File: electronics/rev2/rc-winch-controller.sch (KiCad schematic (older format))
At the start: 14 parts, among them J1 Conn_01x06, J2 Conn_01x06, SW1 SETUP, U1 MCP1703A-3302_SOT23, U2 LPC812M001JDH16, U3 RZ7889

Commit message: Update PCB
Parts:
- removed C4: CP, Capacitor_THT:CP_Axial_L11.0mm_D6.0mm_P18.00mm_Horizontal, symbol Device:CP
- C1, C2: footprint Capacitor_SMD:C_0805_2012Metric_Pad1.18x1.45mm_HandSolder -> Capacitor_SMD:C_0805_2012Metric
- C3: footprint Capacitor_SMD:C_0603_1608Metric_Pad1.08x0.95mm_HandSolder -> Capacitor_SMD:C_0603_1608Metric
- D1: footprint Package_TO_SOT_SMD:SOT-523 -> Package_TO_SOT_SMD:SOT-23
- U1: footprint Package_TO_SOT_SMD:SOT-23_Handsoldering -> Package_TO_SOT_SMD:SOT-23W
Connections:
- net GND: now also J1.5 (Pin_5)
- net LED-A: now also RN1.1 (R1.1); no longer RN1.3 (R3.1)
- net LED-B: now also U2.6 (PIO0_2); no longer U2.9 (PIO0_1)
- net LED-G: now also U2.5 (PIO0_3); no longer U2.6 (PIO0_2)
- net LED-R: now also U2.1 (PIO0_13); no longer U2.5 (PIO0_3)
- net MOT1: now also J2.2 (Pin_2); no longer J2.1 (Pin_1)
- net MOT2: now also J2.1 (Pin_1); no longer J2.2 (Pin_2)
- net Tx: now also RN1.5 (R4.2); no longer RN1.8 (R1.2)
- net Tx-in: now also RN1.4 (R4.1); no longer RN1.1 (R1.1)
- net VDD: now also RN1.8 (R1.2); no longer RN1.6 (R3.2)
- net VMOT: now also J1.6 (Pin_6)
- net ST-Rx renamed AUX-Rx
- net AUX-Rx: now also RN1.6 (R3.2); no longer RN1.5 (R4.2)
- net ST-Rx-in renamed AUX-Rx-in
- net AUX-Rx-in: now also RN1.3 (R3.1); no longer RN1.4 (R4.1)
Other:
- note added: "Pin 5+6 to connect 100uF/16V polymer"
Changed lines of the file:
@@
 F 0 "U1" H 2400 1742 50  0000 C CNN
 F 1 "MCP1703A-3302_SOT23" H 2400 1651 50  0000 C CNN
-F 2 "Package_TO_SOT_SMD:SOT-23_Handsoldering" H 2400 1700 50  0001 C CNN
+F 2 "Package_TO_SOT_SMD:SOT-23W" H 2400 1700 50  0001 C CNN
 F 3 "http://ww1.microchip.com/downloads/en/DeviceDoc/20005122B.pdf" H 2400 1450 50  0001 C CNN
 	1    2400 1500
 	1    0    0    -1
-$EndComp
-$Comp
-L Device:CP C4
-U 1 1 600D9E9B
-P 8000 2800
-F 0 "C4" H 7882 2754 50  0000 R CNN
-F 1 "CP" H 7882 2845 50  0000 R CNN
-F 2 "Capacitor_THT:CP_Axial_L11.0mm_D6.0mm_P18.00mm_Horizontal" H 8038 2650 50  0001 C CNN
-F 3 "~" H 8000 2800 50  0001 C CNN
-	1    8000 2800
-	-1   0    0    1
 $EndComp
 $Comp
@@
 F 0 "C1" H 1865 1696 50  0000 L CNN
 F 1 "1u" H 1865 1605 50  0000 L CNN
-F 2 "Capacitor_SMD:C_0805_2012Metric_Pad1.18x1.45mm_HandSolder" H 1788 1500 50  0001 C CNN
+F 2 "Capacitor_SMD:C_0805_2012Metric" H 1788 1500 50  0001 C CNN
 F 3 "~" H 1750 1650 50  0001 C CNN
 	1    1750 1650
@@
 F 0 "C2" H 3165 1696 50  0000 L CNN
 F 1 "10u" H 3165 1605 50  0000 L CNN
-F 2 "Capacitor_SMD:C_0805_2012Metric_Pad1.18x1.45mm_HandSolder" H 3088 1500 50  0001 C CNN
+F 2 "Capacitor_SMD:C_0805_2012Metric" H 3088 1500 50  0001 C CNN
 F 3 "~" H 3050 1650 50  0001 C CNN
 	1    3050 1650
@@
 F 0 "C3" H 3565 1696 50  0000 L CNN
 F 1 "100n" H 3565 1605 50  0000 L CNN
-F 2 "Capacitor_SMD:C_0603_1608Metric_Pad1.08x0.95mm_HandSolder" H 3488 1500 50  0001 C CNN
+F 2 "Capacitor_SMD:C_0603_1608Metric" H 3488 1500 50  0001 C CNN
 F 3 "~" H 3450 1650 50  0001 C CNN
 	1    3450 1650
@@
 $EndComp
 Wire Wire Line
-	6500 5200 6050 5200
-Wire Wire Line
-	6050 5300 6350 5300
-Wire Wire Line
-	6900 5200 7450 5200
-Wire Wire Line
-	7450 5300 7000 5300
+	6500 5200 6350 5200
+Wire Wire Line
+	6900 5200 7000 5200
 Wire Wire Line
 	4150 3250 3600 3250
 Text Label 3600 3250 0    50   ~ 0
-ST-Rx
+AUX-Rx
 Wire Wire Line
 	4150 3650 3600 3650
@@
 Wire Wire Line
 	7400 2950 7400 3050
-Connection ~ 8000 2950
-Wire Wire Line
-	8000 2950 7400 2950
-$Comp
-L power:GND #PWR09
-U 1 1 600FB047
-P 8000 2550
-F 0 "#PWR09" H 8000 2300 50  0001 C CNN
-F 1 "GND" H 8005 2377 50  0000 C CNN
-F 2 "" H 8000 2550 50  0001 C CNN
-F 3 "" H 8000 2550 50  0001 C CNN
-	1    8000 2550
-	-1   0    0    1
-$EndComp
-Wire Wire Line
-	8000 2550 8000 2650
 $Comp
 L Device:D_Schottky_x2_KCom_AAK D1
@@
 F 0 "D1" H 1750 1167 50  0000 C CNN
 F 1 "D_Schottky_x2_KCom_AAK" H 1750 1076 50  0000 C CNN
-F 2 "Package_TO_SOT_SMD:SOT-523" H 1750 950 50  0001 C CNN
+F 2 "Package_TO_SOT_SMD:SOT-23" H 1750 950 50  0001 C CNN
 F 3 "~" H 1750 950 50  0001 C CNN
 	1    1750 950
@@
 Text Label 1100 950  0    50   ~ 0
 VMOT
-Text Label 7500 2950 0    50   ~ 0
+Text Label 7950 2950 0    50   ~ 0
 VMOT
 Wire Wire Line
@@
 Wire Wire Line
 	7400 3950 7400 4050
-Wire Wire Line
-	6900 5400 7000 5400
-Wire Wire Line
-	6500 5400 6350 5400
-Text Label 6050 5300 0    50   ~ 0
+Text Label 6050 5200 0    50   ~ 0
 LED-A
 Wire Wire Line
@@
 Wire Wire Line
 	3600 3450 4150 3450
+Text Label 3600 3550 0    50   ~ 0
+LED-G
+Text Label 6150 3850 2    50   ~ 0
+LED-R
 Text Label 3600 3450 0    50   ~ 0
-LED-G
-Text Label 3600 3550 0    50   ~ 0
-LED-R
-Wire Wire Line
-	3600 3350 4150 3350
-Text Label 3600 3350 0    50   ~ 0
 LED-B
 Text Label 4200 1500 0    50   ~ 0
 VDD
-Text Label 7450 5300 2    50   ~ 0
+Text Label 7450 5200 2    50   ~ 0
 VDD
+Text Label 6050 5400 0    50   ~ 0
+AUX-Rx-in
 Text Label 6050 5500 0    50   ~ 0
-ST-Rx-in
-Text Label 6050 5200 0    50   ~ 0
 Tx-in
+Text Label 7450 5400 2    50   ~ 0
+AUX-Rx
 Text Label 7450 5500 2    50   ~ 0
-ST-Rx
-Text Label 7450 5200 2    50   ~ 0
 Tx
 Wire Wire Line
@@
 	1950 3150 1350 3150
 Text Label 1950 3250 2    50   ~ 0
-ST-Rx-in
+AUX-Rx-in
 Text Label 1950 3150 2    50   ~ 0
 Tx-in
@@
 	0    1    1    0
 $EndComp
-Wire Wire Line
-	8500 2950 8000 2950
-NoConn ~ 1350 3050
 Text Label 9150 2950 0    50   ~ 0
 VMOT-in
 Text Notes 5800 5750 0    50   ~ 0
 2x 1k in parallel to get detect LED current
-NoConn ~ 1350 2950
 Wire Wire Line
 	7800 3350 7900 3350
@@
 U 1 1 6019C61D
 P 7400 3450
-F 0 "U3" H 7400 4031 50  0000 C CNN
-F 1 "RZ7889" H 7400 3940 50  0000 C CNN
+F 0 "U3" H 7650 3800 50  0000 C CNN
+F 1 "RZ7889" H 7150 3800 50  0000 C CNN
 F 2 "Package_SO:SOIC-8-1EP_3.9x4.9mm_P1.27mm_EP2.29x3mm_ThermalVias" H 7400 2900 50  0001 C CNN
 F 3 "" H 7100 3800 50  0001 C CNN
@@
 Text Label 6450 3250 0    50   ~ 0
 FWD
-Wire Wire Line
-	8650 3250 8650 3350
-Wire Wire Line
-	8650 3350 9550 3350
-Wire Wire Line
-	7900 3250 8650 3250
 Connection ~ 7900 3250
-Wire Wire Line
-	9550 3250 8850 3250
-Wire Wire Line
-	8850 3250 8850 3450
 Wire Wire Line
 	8850 3450 8100 3450
@@
 LED-A
 Wire Wire Line
-	6350 5400 6350 5300
-Connection ~ 6350 5300
-Wire Wire Line
 	6350 5300 6500 5300
 Wire Wire Line
 	6050 5500 6500 5500
 Wire Wire Line
-	7000 5400 7000 5300
-Connection ~ 7000 5300
-Wire Wire Line
 	7000 5300 6900 5300
 Wire Wire Line
 	6900 5500 7450 5500
+Wire Wire Line
+	1350 3050 1500 3050
+Wire Wire Line
+	1500 3050 1500 3450
+Connection ~ 1500 3450
+Wire Wire Line
+	1350 2950 1950 2950
+Text Label 1950 2950 2    50   ~ 0
+VMOT
+Wire Wire Line
+	7400 2950 8500 2950
+Text Notes 850  4050 0    50   ~ 0
+Pin 5+6 to connect 100uF/16V polymer
+Wire Wire Line
+	6350 5200 6350 5300
+Connection ~ 6350 5200
+Wire Wire Line
+	6350 5200 6050 5200
+Wire Wire Line
+	6050 5400 6500 5400
+Wire Wire Line
+	7000 5300 7000 5200
+Connection ~ 7000 5200
+Wire Wire Line
+	7000 5200 7450 5200
+Wire Wire Line
+	6900 5400 7450 5400
+Wire Wire Line
+	7900 3250 9550 3250
+Wire Wire Line
+	8850 3450 8850 3350
+Wire Wire Line
+	8850 3350 9550 3350
+Wire Wire Line
+	6150 3850 5550 3850
+NoConn ~ 4150 3350
+NoConn ~ 4150 3750
 $EndSCHEMATC

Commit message: Update layout and silkscreen
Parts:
- F1: value 3A 16V 1812 -> 4A 16V 1812
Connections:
- net AUX-Rx: now also RN1.5 (R4.2); no longer RN1.6 (R3.2)
- net AUX-Rx-in: now also RN1.4 (R4.1); no longer RN1.3 (R3.1)
- net Tx: now also RN1.6 (R3.2); no longer RN1.5 (R4.2)
- net Tx-in: now also RN1.3 (R3.1); no longer RN1.4 (R4.1)
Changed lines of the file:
@@
 Text Label 7450 5200 2    50   ~ 0
 VDD
+Text Label 6050 5500 0    50   ~ 0
+AUX-Rx-in
 Text Label 6050 5400 0    50   ~ 0
-AUX-Rx-in
-Text Label 6050 5500 0    50   ~ 0
 Tx-in
+Text Label 7450 5500 2    50   ~ 0
+AUX-Rx
 Text Label 7450 5400 2    50   ~ 0
-AUX-Rx
-Text Label 7450 5500 2    50   ~ 0
 Tx
 Wire Wire Line
@@
 P 8650 2950
 F 0 "F1" V 8425 2950 50  0000 C CNN
-F 1 "3A 16V 1812" V 8516 2950 50  0000 C CNN
+F 1 "4A 16V 1812" V 8516 2950 50  0000 C CNN
 F 2 "Fuse:Fuse_1812_4532Metric_Pad1.30x3.40mm_HandSolder" H 8700 2750 50  0001 L CNN
 F 3 "~" H 8650 2950 50  0001 C CNN

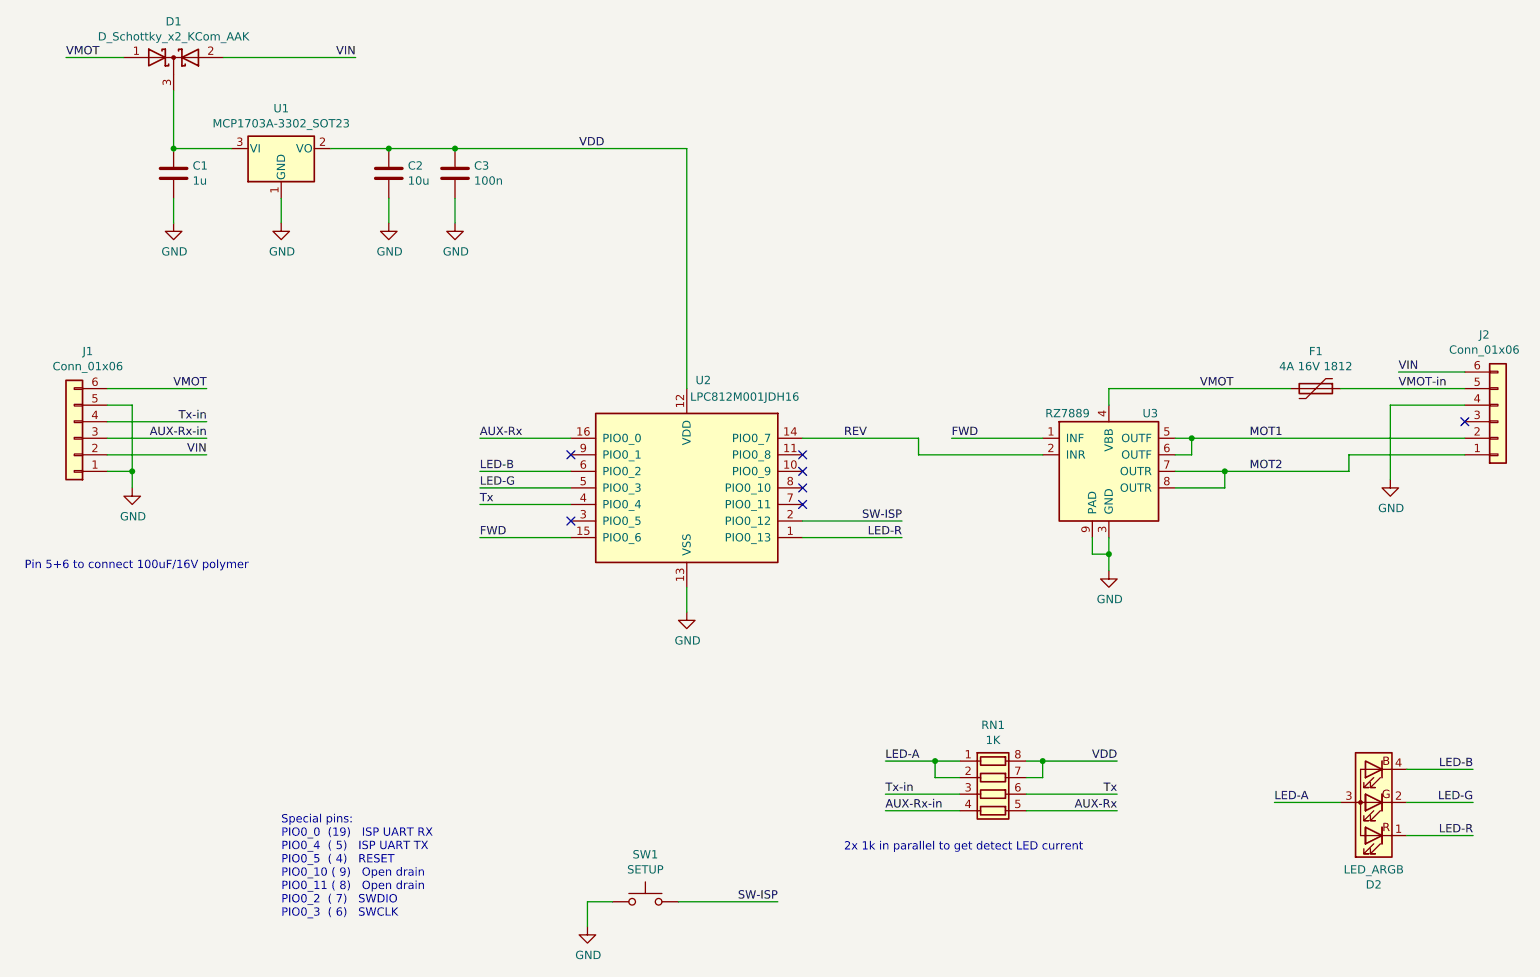
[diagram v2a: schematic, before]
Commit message: Change MCU to TSSOP 20 version
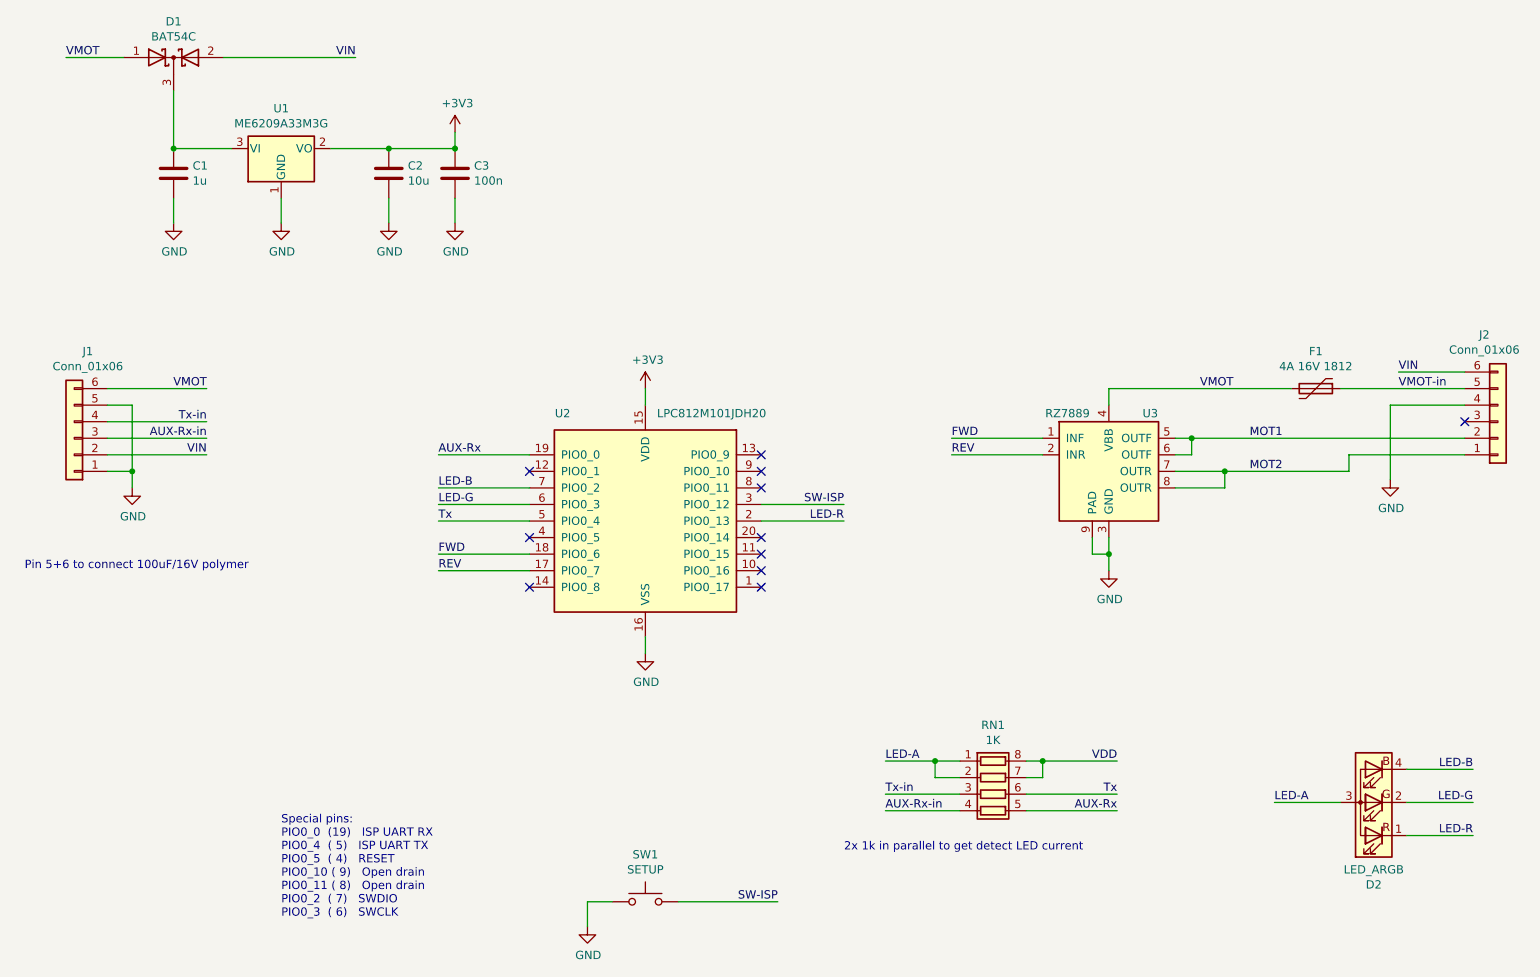
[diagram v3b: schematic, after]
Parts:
- removed U2: LPC812M001JDH16, Package_SO:TSSOP-16_4.4x5mm_P0.65mm, symbol MCU_NXP_LPC:LPC812M001JDH16
- added U2: LPC812M101JDH20, Package_SO:TSSOP-20_4.4x6.5mm_P0.65mm, symbol MCU_NXP_LPC:LPC812M101JDH20
- D1: value D_Schottky_x2_KCom_AAK -> BAT54C
- U1: value MCP1703A-3302_SOT23 -> ME6209A33M3G
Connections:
- net AUX-Rx: now also U2.19 (PIO0_0)
- net FWD: now also U2.18 (PIO0_6)
- net GND: now also U2.16 (VSS)
- net LED-B: now also U2.7 (PIO0_2)
- net LED-G: now also U2.6 (PIO0_3)
- net LED-R: now also U2.2 (PIO0_13)
- net REV: now also U2.17 (PIO0_7)
- net SW-ISP: now also U2.3 (PIO0_12)
- net Tx: now also U2.5 (PIO0_4)
- net VDD: no longer C2.1, C3.1, U1.2 (VO)
- new net +3V3: C2.1, C3.1, U1.2 (VO), U2.15 (VDD)
- no-connect marks 7 -> 11
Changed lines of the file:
@@
 Sheet 1 1
 Title "RC Winch Controller"
-Date "2021-01-24"
+Date "2021-02-11"
 Rev "Rev2"
 Comp "LANE Boys RC"
@@
 Comment4 ""
 $EndDescr
-$Comp
-L MCU_NXP_LPC:LPC812M001JDH16 U2
-U 1 1 600D3394
-P 4850 3550
-F 0 "U2" H 4950 4200 50  0000 C CNN
-F 1 "LPC812M001JDH16" H 5200 4100 50  0000 C CNN
-F 2 "Package_SO:TSSOP-16_4.4x5mm_P0.65mm" H 5800 4150 50  0001 C CNN
-F 3 "http://www.nxp.com/documents/data_sheet/LPC81XM.pdf" H 4850 3050 50  0001 C CNN
-	1    4850 3550
-	1    0    0    -1
-$EndComp
 $Comp
 L rc-winch-controller-parts:XINLIGHT_XL-2012RGBC D2
@@
 P 2400 1500
 F 0 "U1" H 2400 1742 50  0000 C CNN
-F 1 "MCP1703A-3302_SOT23" H 2400 1651 50  0000 C CNN
+F 1 "ME6209A33M3G" H 2400 1651 50  0000 C CNN
 F 2 "Package_TO_SOT_SMD:SOT-23W" H 2400 1700 50  0001 C CNN
 F 3 "http://ww1.microchip.com/downloads/en/DeviceDoc/20005122B.pdf" H 2400 1450 50  0001 C CNN
@@
 Wire Wire Line
 	6900 5200 7000 5200
-Wire Wire Line
-	4150 3250 3600 3250
-Text Label 3600 3250 0    50   ~ 0
-AUX-Rx
-Wire Wire Line
-	4150 3650 3600 3650
-Text Label 3600 3650 0    50   ~ 0
-Tx
-Wire Wire Line
-	5550 3750 6150 3750
-Text Label 6150 3750 2    50   ~ 0
-SW-ISP
-$Comp
-L power:GND #PWR07
-U 1 1 600ED009
-P 4850 4300
-F 0 "#PWR07" H 4850 4050 50  0001 C CNN
-F 1 "GND" H 4855 4127 50  0000 C CNN
-F 2 "" H 4850 4300 50  0001 C CNN
-F 3 "" H 4850 4300 50  0001 C CNN
-	1    4850 4300
-	1    0    0    -1
-$EndComp
-Wire Wire Line
-	4850 4150 4850 4300
 $Comp
 L power:GND #PWR06
@@
 Text Notes 2400 6150 0    50   ~ 0
 Special pins:\nPIO0_0  (19)   ISP UART RX\nPIO0_4  ( 5)   ISP UART TX\nPIO0_5  ( 4)   RESET\nPIO0_10 ( 9)   Open drain\nPIO0_11 ( 8)   Open drain\nPIO0_2  ( 7)   SWDIO\nPIO0_3  ( 6)   SWCLK
-Text Label 3600 3850 0    50   ~ 0
-FWD
-Text Label 5800 3250 0    50   ~ 0
-REV
 Wire Wire Line
 	7800 3250 7900 3250
@@
 P 1750 950
 F 0 "D1" H 1750 1167 50  0000 C CNN
-F 1 "D_Schottky_x2_KCom_AAK" H 1750 1076 50  0000 C CNN
+F 1 "BAT54C" H 1750 1076 50  0000 C CNN
 F 2 "Package_TO_SOT_SMD:SOT-23" H 1750 950 50  0001 C CNN
 F 3 "~" H 1750 950 50  0001 C CNN
@@
 Wire Wire Line
 	2700 1500 3050 1500
-Wire Wire Line
-	4850 1500 4850 2950
 Connection ~ 3050 1500
 Wire Wire Line
 	3050 1500 3450 1500
 Connection ~ 3450 1500
-Wire Wire Line
-	3450 1500 4850 1500
 Connection ~ 1750 1500
 $Comp
@@
 Text Label 9600 5250 2    50   ~ 0
 LED-B
-NoConn ~ 5550 3550
-NoConn ~ 5550 3650
-Wire Wire Line
-	4150 3550 3600 3550
-Wire Wire Line
-	3600 3450 4150 3450
-Text Label 3600 3550 0    50   ~ 0
-LED-G
-Text Label 6150 3850 2    50   ~ 0
-LED-R
-Text Label 3600 3450 0    50   ~ 0
-LED-B
-Text Label 4200 1500 0    50   ~ 0
-VDD
 Text Label 7450 5200 2    50   ~ 0
 VDD
@@
 $EndComp
 Wire Wire Line
-	3600 3850 4150 3850
-NoConn ~ 5550 3350
-NoConn ~ 5550 3450
-Wire Wire Line
-	5550 3250 6250 3250
-Wire Wire Line
-	6250 3250 6250 3350
-Wire Wire Line
-	6250 3350 7000 3350
+	6450 3350 7000 3350
 Wire Wire Line
 	6450 3250 7000 3250
@@
 Wire Wire Line
 	8850 3350 9550 3350
-Wire Wire Line
-	6150 3850 5550 3850
-NoConn ~ 4150 3350
-NoConn ~ 4150 3750
+$Comp
+L power:+3V3 #PWR?
+U 1 1 60252048
+P 3450 1400
+F 0 "#PWR?" H 3450 1250 50  0001 C CNN
+F 1 "+3V3" H 3465 1573 50  0000 C CNN
+F 2 "" H 3450 1400 50  0001 C CNN
+F 3 "" H 3450 1400 50  0001 C CNN
+	1    3450 1400
+	1    0    0    -1
+$EndComp
+Wire Wire Line
+	3450 1400 3450 1500
+Text Label 6450 3350 0    50   ~ 0
+REV
+$Comp
+L MCU_NXP_LPC:LPC812M101JDH20 U2
+U 1 1 60268FFA
+P 4600 3750
+F 0 "U2" H 4100 4400 50  0000 C CNN
+F 1 "LPC812M101JDH20" H 5000 4400 50  0000 C CNN
+F 2 "Package_SO:TSSOP-20_4.4x6.5mm_P0.65mm" H 5600 4450 50  0001 C CNN
+F 3 "http://www.nxp.com/documents/data_sheet/LPC81XM.pdf" H 4600 3250 50  0001 C CNN
+	1    4600 3750
+	1    0    0    -1
+$EndComp
+$Comp
+L power:+3V3 #PWR?
+U 1 1 6026DDF4
+P 4600 2950
+F 0 "#PWR?" H 4600 2800 50  0001 C CNN
+F 1 "+3V3" H 4615 3123 50  0000 C CNN
+F 2 "" H 4600 2950 50  0001 C CNN
+F 3 "" H 4600 2950 50  0001 C CNN
+	1    4600 2950
+	1    0    0    -1
+$EndComp
+Wire Wire Line
+	4600 2950 4600 3050
+$Comp
+L power:GND #PWR?
+U 1 1 6026FF95
+P 4600 4550
+F 0 "#PWR?" H 4600 4300 50  0001 C CNN
+F 1 "GND" H 4605 4377 50  0000 C CNN
+F 2 "" H 4600 4550 50  0001 C CNN
+F 3 "" H 4600 4550 50  0001 C CNN
+	1    4600 4550
+	1    0    0    -1
+$EndComp
+Wire Wire Line
+	4600 4450 4600 4550
+Wire Wire Line
+	3900 3350 3350 3350
+Text Label 3350 3350 0    50   ~ 0
+AUX-Rx
+Wire Wire Line
+	3900 3750 3350 3750
+Text Label 3350 3750 0    50   ~ 0
+Tx
+Text Label 3350 3950 0    50   ~ 0
+FWD
+Wire Wire Line
+	3900 3650 3350 3650
+Wire Wire Line
+	3350 3550 3900 3550
+Text Label 3350 3650 0    50   ~ 0
+LED-G
+Text Label 3350 3550 0    50   ~ 0
+LED-B
+Wire Wire Line
+	3350 3950 3900 3950
+Text Label 3350 4050 0    50   ~ 0
+REV
+Wire Wire Line
+	3900 4050 3350 4050
+NoConn ~ 3900 3450
+NoConn ~ 3900 3850
+NoConn ~ 3900 4150
+Wire Wire Line
+	5300 3650 5800 3650
+Text Label 5800 3650 2    50   ~ 0
+SW-ISP
+Text Label 5800 3750 2    50   ~ 0
+LED-R
+Wire Wire Line
+	5800 3750 5300 3750
+NoConn ~ 5300 3350
+NoConn ~ 5300 3450
+NoConn ~ 5300 3550
+NoConn ~ 5300 3850
+NoConn ~ 5300 3950
+NoConn ~ 5300 4050
+NoConn ~ 5300 4150
 $EndSCHEMATC
